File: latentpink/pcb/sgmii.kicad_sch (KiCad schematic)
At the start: 4 parts, among them J22 BEL_FUSE_0845-2R1T-E4, U2 XC7K160T-2FBG484C, U5 DP83867, U6 DP83867

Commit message: Initial start of DP83867 schematic
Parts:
- added C355, C356, C365, C366, C367, C368, C369, C370, C371, C372, C373, C374, C375, C376, C377, C378, C379, C380, C381, C382, C383, C384, C385, C386: 0.47 uF, azonenberg_pcb:EIA_0402_CAP_NOSILK, symbol device:C
- added C357, C358, C359, C360, C361, C362, C363, C364: 4.7 uF, azonenberg_pcb:EIA_0603_CAP_NOSILK, symbol device:C
- added R112, R?: 1.5K, symbol device:R
- added R113, R?: 2.2K, symbol device:R
- added R114, R?: 11K 1%, symbol device:R
- added R115, R116: 33, azonenberg_pcb:EIA_0402_RES_NOSILK, symbol device:R
- added R? (x2): R, symbol device:R
- added TP21, TP22: TESTPOINT, symbol conn:CONN_01X01
- added U7, U8: TBD, symbol osc-azonenberg:OSC
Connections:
- net GND: now reaches J22.1 (GND)
- net GND: now also J22.20 (GND), U5.PAD (GND), U6.PAD (GND), C355.2, C356.2, C357.2, C358.2, C359.2, C360.2, C361.2, C362.2, C363.2, C364.2, C365.2, C366.2, C367.2, C368.2, C369.2, C370.2, C371.2, C372.2, C373.2, C374.2, C375.2, C376.2, C377.2, C378.2, C379.2, C380.2, C381.2, C382.2, C383.2, C384.2, C385.2, C386.2, R114.1, R?.1, U7.2 (Vss), U8.2 (Vss)
- net ETH13_C_N: now reaches J22.10 (BI_DC_N)
- net ETH13_C_N: now also U5.8 (ETH_C_N)
- net ETH13_B_P: now reaches J22.11 (BI_DB_P)
- net ETH13_B_P: now also U5.4 (ETH_B_P)
- net ETH13_A_N: now reaches J22.13 (BI_DA_N)
- net ETH13_A_N: now also U5.2 (ETH_A_N)
- net ETH13_D_N: now reaches J22.2 (BI_DD_N)
- net ETH13_D_N: now also U5.11 (ETH_D_N)
- net ETH13_C_P: now reaches J22.3 (BI_DC_P)
- net ETH13_C_P: now also U5.7 (ETH_C_P)
- net ETH13_B_N: now reaches J22.5 (BI_DB_N)
- net ETH13_B_N: now also U5.5 (ETH_B_N)
- net ETH13_A_P: now reaches J22.6 (BI_DA_P)
- net ETH13_A_P: now also U5.1 (ETH_A_P)
- net ETH13_D_P: now reaches J22.9 (BI_DD_P)
- net ETH13_D_P: now also U5.10 (ETH_D_P)
- net ETH12_A_P: now reaches U6.1 (ETH_A_P)
- net ETH12_D_P: now reaches U6.10 (ETH_D_P)
- net ETH12_D_P: now also J22.26 (BI_DD_P)
- net ETH12_D_N: now reaches U6.11 (ETH_D_N)
- net ETH12_D_N: now also J22.19 (BI_DD_N)
- net at U6.12 (RBIAS): now also R114.2
- net DP_A1V8: now reaches U6.13 (A1V8)
- net DP_A1V8: now also U5.13 (A1V8), U5.48 (A1V8), U6.48 (A1V8), C359.1, C363.1, C367.1, C371.1, C374.1, C377.1
- net PHY_CLK_25MHZ_0: now reaches U6.15 (XI)
- net PHY_CLK_25MHZ_0: now also R115.2
- net DP_MDC: now reaches U6.16 (MDC)
- net DP_MDC: now also U2.AA6 (IO_L3P_T0_DQS_33), U5.16 (MDC)
- net DP_MDIO: now reaches U6.17 (MDIO)
- net DP_MDIO: now also U2.AB6 (IO_L3N_T0_DQS_33), U5.17 (MDIO), R112.2, R?.2
- net DP_CLKOUT0: now reaches U6.18 (CLK_OUT)
- net DP_CLKOUT0: now also TP21.1 (P1)
- net 1V8: now reaches U6.19 (VCCIO)
- net 1V8: now also U5.19 (VCCIO), U5.30 (VCCIO), U5.41 (VCCIO), U6.30 (VCCIO), U6.41 (VCCIO), C355.1, C356.1, R112.1, R113.1, R?.1, R?.1, U7.1 (E/D#), U7.4 (Vdd), U8.1 (E/D#), U8.4 (Vdd)
- net ETH12_A_N: now reaches U6.2 (ETH_A_N)
- net ETH12_A_N: now also J22.15 (BI_DA_P), J22.21 (BI_DA_N)
- net 1V0: now reaches U6.24 (1V0)
- net 1V0: now also U5.24 (1V0), U5.31 (1V0), U5.42 (1V0), U5.6 (1V0), U6.31 (1V0), U6.42 (1V0), U6.6 (1V0), C358.1, C362.1, C366.1, C370.1, C373.1, C376.1, C381.1, C383.1, C385.1, C386.1
- net ETH12_SGMII_TX_P: now reaches U6.27 (TX_D1/SGMII_TX_P)
- net ETH12_SGMII_TX_N: now reaches U6.28 (TX_D0/SGMII_TX_N)
- net DP_A2V5: now reaches U6.3 (A2V5)
- net DP_A2V5: now also U5.3 (A2V5), U5.9 (A2V5), U6.9 (A2V5), C357.1, C361.1, C365.1, C369.1, C379.1, C380.1
- net ETH12_SGMII_CLKOUT_P: now reaches U6.33 (RX_D0/SGMII_CLKOUT_P)
- net ETH12_SGMII_CLKOUT_N: now reaches U6.34 (RX_D1/SGMII_CLKOUT_N)
- net ETH12_SGMII_RX_P: now reaches U6.35 (RX_D2/SGMII_RX_P)
- net ETH12_SGMII_RX_N: now reaches U6.36 (RX_D3/SGMII_RX_N)
- net ETH12_RX_CTRL_STRAP: now reaches U6.38 (RX_CTRL)
- net ETH12_B_P: now reaches U6.4 (ETH_B_P)
- net ETH12_B_P: now also J22.23 (BI_DB_P)
- net ETH12_RST_N: now reaches U6.43 (~{RESET})
- net ETH12_RST_N: now also U2.AB7 (IO_L2N_T0_33)
- net ETH12_INT_N: now reaches U6.44 (~{INT}/~{PWRDN})
- net ETH12_INT_N: now also U2.AB8 (IO_L2P_T0_33), R113.2
- net ETH12_B_N: now reaches U6.5 (ETH_B_N)
- net ETH12_B_N: now also J22.16 (BI_DB_N)
- net ETH12_C_P: now reaches U6.7 (ETH_C_P)
- net ETH12_C_P: now also J22.18 (BI_DC_P)
- net ETH12_C_N: now reaches U6.8 (ETH_C_N)
- net ETH12_C_N: now also J22.24 (BI_DC_N)
- net at U5.12 (RBIAS): now also R?.2
- net PHY_CLK_25MHZ_1: now reaches U5.15 (XI)
- net PHY_CLK_25MHZ_1: now also R116.2
- net DP_CLKOUT1: now reaches U5.18 (CLK_OUT)
- net DP_CLKOUT1: now also TP22.1 (P1)
- net ETH13_SGMII_TX_P: now reaches U5.27 (TX_D1/SGMII_TX_P)
- net ETH13_SGMII_TX_N: now reaches U5.28 (TX_D0/SGMII_TX_N)
- net ETH13_SGMII_CLKOUT_P: now reaches U5.33 (RX_D0/SGMII_CLKOUT_P)
- net ETH13_SGMII_CLKOUT_N: now reaches U5.34 (RX_D1/SGMII_CLKOUT_N)
- net ETH13_SGMII_RX_P: now reaches U5.35 (RX_D2/SGMII_RX_P)
- net ETH13_SGMII_RX_N: now reaches U5.36 (RX_D3/SGMII_RX_N)
- net ETH13_RX_CTRL_STRAP: now reaches U5.38 (RX_CTRL)
- net ETH13_RST_N: now reaches U5.43 (~{RESET})
- net ETH13_RST_N: now also U2.AB5 (IO_L1N_T0_33)
- net ETH13_INT_N: now reaches U5.44 (~{INT}/~{PWRDN})
- net ETH13_INT_N: now also U2.AA5 (IO_L1P_T0_33), R?.2
- net at U2.T14 (IO_25_VRP_33): now also R?.2
- net at U2.T6 (IO_0_VRN_33): now also R?.2
- net CHGND: now reaches J22.SHLD
- new net: R116.1, U8.3 (CLK)
- new net: R115.1, U7.3 (CLK)
- new net D1V8: C360.1, C364.1, C368.1, C372.1, C375.1, C378.1, C382.1, C384.1
- no-connect marks 0 -> 12
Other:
- note added: "TODO: PHYADDR straps"
- note added: "TODO: ac coupling and/or biasing"
- note added: "TODO: power filtering"
- moved on the sheet: U2G

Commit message: Rearranged ports, added center tap capacitors
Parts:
- added C387, C388, C389, C390, C391, C392: 0.1 uF, azonenberg_pcb:EIA_0402_CAP_NOSILK, symbol device:C
- R117, R118: renamed from R?; value R -> 100
- gave numbers to parts that had none: 3
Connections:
- net D1V8 is gone; now on net 1V8_IO: C360.1, C364.1, C368.1, C372.1, C375.1, C378.1, C382.1, C384.1
- net 1V8: no longer C355.1, C356.1, U5.19 (VCCIO), U5.30 (VCCIO), U5.41 (VCCIO), U6.19 (VCCIO), U6.30 (VCCIO), U6.41 (VCCIO), U7.1 (E/D#), U7.4 (Vdd), U8.1 (E/D#), U8.4 (Vdd)
- net ETH12_SGMII_CLKOUT_N: now also C390.1
- net ETH12_SGMII_CLKOUT_P: now also C389.1
- net ETH12_SGMII_RX_N: now also C392.1
- net ETH12_SGMII_RX_P: now also C391.1
- net ETH12_SGMII_TX_N: now also C388.1
- net ETH12_SGMII_TX_P: now also C387.1
- net GND: now also R118.1
- net 1V8_IO: now reaches R117.1
- net 1V8_IO: now also C355.1, C356.1, U5.19 (VCCIO), U5.30 (VCCIO), U5.41 (VCCIO), U6.19 (VCCIO), U6.30 (VCCIO), U6.41 (VCCIO), U7.1 (E/D#), U7.4 (Vdd), U8.1 (E/D#), U8.4 (Vdd)
- net ETH12_SGMII_RX_AC_N: now reaches U2.U6 (IO_L10N_T1_33)
- net ETH12_SGMII_RX_AC_N: now also C392.2
- net ETH12_SGMII_RX_AC_P: now reaches U2.U7 (IO_L10P_T1_33)
- net ETH12_SGMII_RX_AC_P: now also C391.2
- net ETH12_SGMII_TX_AC_P: now reaches U2.V7 (IO_L11P_T1_SRCC_33)
- net ETH12_SGMII_TX_AC_P: now also C387.2
- net ETH12_SGMII_TX_AC_N: now reaches U2.W7 (IO_L11N_T1_SRCC_33)
- net ETH12_SGMII_TX_AC_N: now also C388.2
- net ETH12_SGMII_CLKOUT_AC_N: now reaches U2.Y7 (IO_L12N_T1_MRCC_33)
- net ETH12_SGMII_CLKOUT_AC_N: now also C390.2
- net ETH12_SGMII_CLKOUT_AC_P: now reaches U2.Y8 (IO_L12P_T1_MRCC_33)
- net ETH12_SGMII_CLKOUT_AC_P: now also C389.2
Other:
- note added: "SGMII AC coupling Hook up clocks just in case, but if we need them something is wrong."
- note added: "UG471 figure 1-10 Ext ref resistor = 2x Z0"
- note added: "Use DIFF_HSTL_I_DCI_18 for SGMII inputs Separate split terminations No biasing needed since termination provides bias to keep Vcm at Vccio/2"
- note removed: "TODO: ac coupling and/or biasing"
- moved on the sheet: R117, R118, U2G

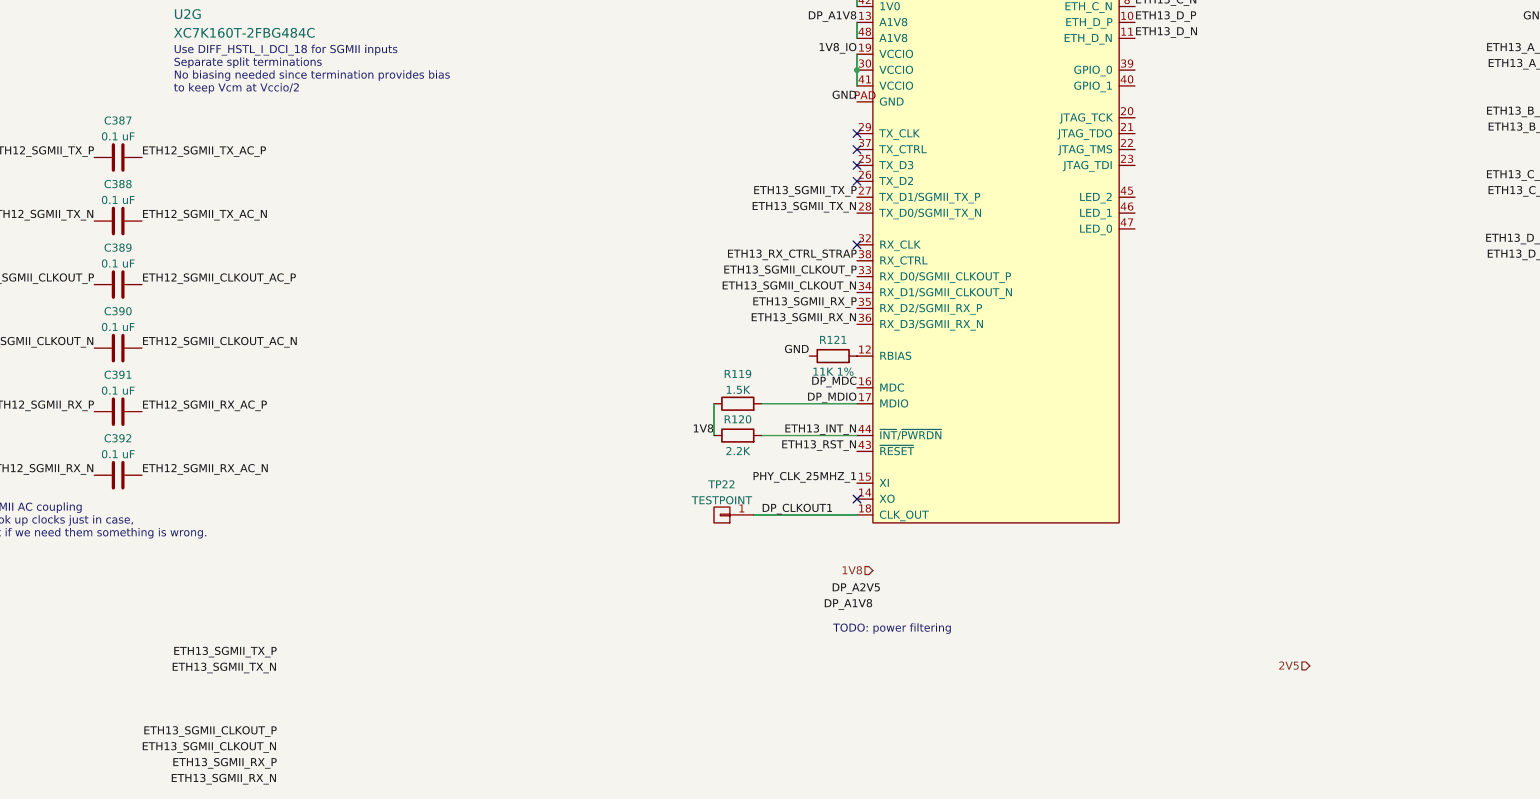
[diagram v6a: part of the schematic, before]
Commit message: Continued initial component placement
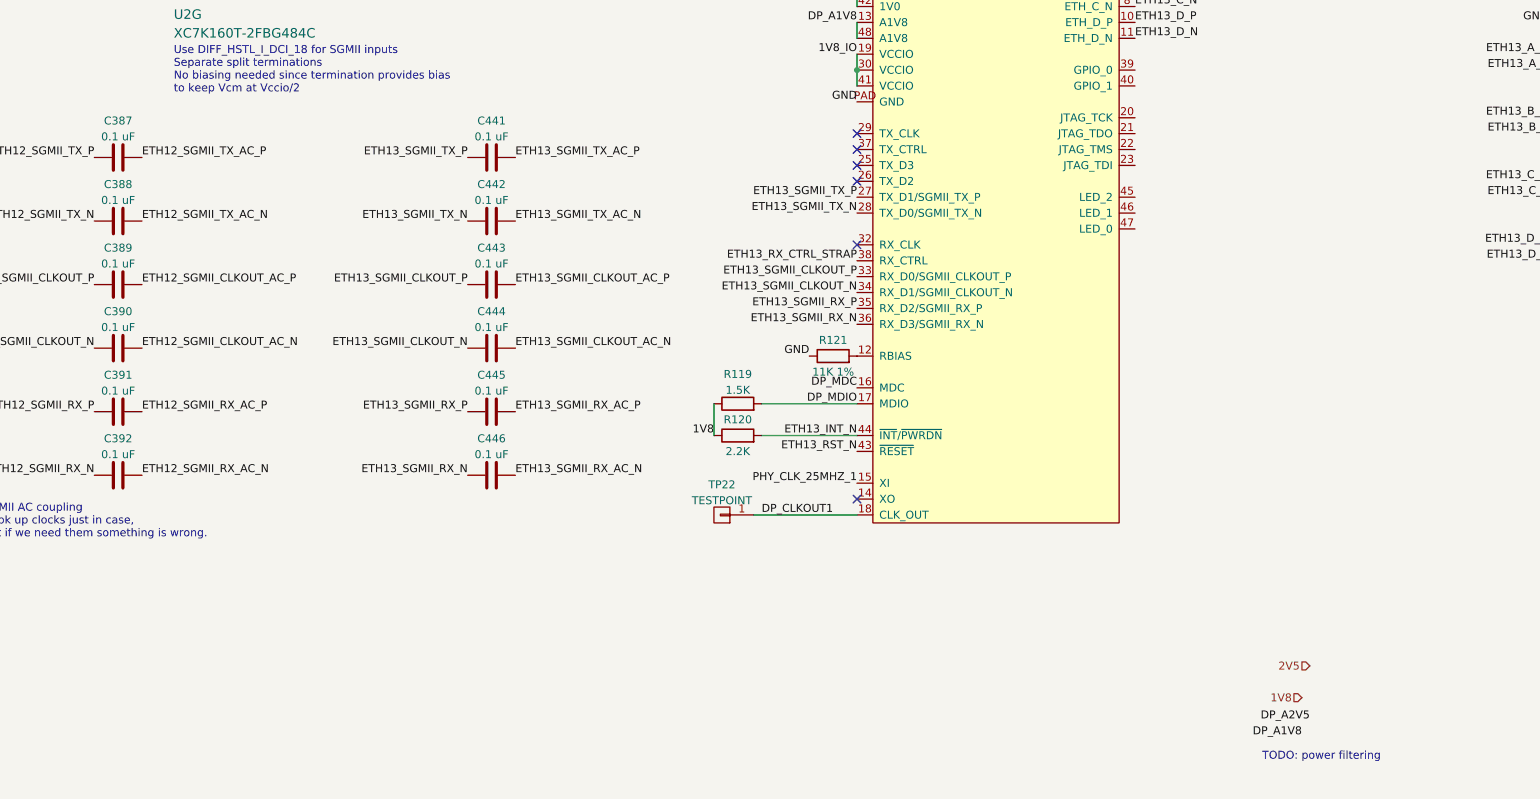
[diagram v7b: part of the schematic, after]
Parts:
- added C441, C442, C443, C444, C445, C446: 0.1 uF, azonenberg_pcb:EIA_0402_CAP_NOSILK, symbol device:C
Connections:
- net ETH13_SGMII_CLKOUT_N: now also C444.1
- net ETH13_SGMII_CLKOUT_P: now also C443.1
- net ETH13_SGMII_RX_N: now also C446.1
- net ETH13_SGMII_RX_P: now also C445.1
- net ETH13_SGMII_TX_N: now also C442.1
- net ETH13_SGMII_TX_P: now also C441.1
- new net ETH13_SGMII_CLKOUT_AC_N: C444.2
- new net ETH13_SGMII_CLKOUT_AC_P: C443.2
- new net ETH13_SGMII_RX_AC_N: C446.2
- new net ETH13_SGMII_RX_AC_P: C445.2
- new net ETH13_SGMII_TX_AC_N: C442.2
- new net ETH13_SGMII_TX_AC_P: C441.2
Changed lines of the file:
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@@
     (effects (font (size 1.27 1.27)) (justify left bottom))
   )
-  (text "TODO: power filtering" (at 154.94 254 0)
+  (text "TODO: power filtering" (at 223.52 274.32 0)
     (effects (font (size 1.27 1.27)) (justify left bottom))
   )
@@
     (effects (font (size 1.27 1.27)) (justify right bottom))
   )
-  (label "ETH13_SGMII_RX_P" (at 66.04 275.59 180)
+  (label "ETH13_SGMII_RX_P" (at 96.52 218.44 180)
     (effects (font (size 1.27 1.27)) (justify right bottom))
   )
@@
     (effects (font (size 1.27 1.27)) (justify right bottom))
   )
+  (label "ETH13_SGMII_TX_AC_P" (at 104.14 177.8 0)
+    (effects (font (size 1.27 1.27)) (justify left bottom))
+  )
   (label "ETH12_SGMII_CLKOUT_AC_N" (at 44.45 208.28 0)
     (effects (font (size 1.27 1.27)) (justify left bottom))
@@
     (effects (font (size 1.27 1.27)) (justify right bottom))
   )
+  (label "ETH13_SGMII_TX_AC_N" (at 104.14 187.96 0)
+    (effects (font (size 1.27 1.27)) (justify left bottom))
+  )
   (label "ETH12_SGMII_RX_P" (at 36.83 218.44 180)
     (effects (font (size 1.27 1.27)) (justify right bottom))
@@
     (effects (font (size 1.27 1.27)) (justify right bottom))
   )
-  (label "ETH13_SGMII_RX_N" (at 66.04 278.13 180)
+  (label "ETH13_SGMII_RX_N" (at 96.52 228.6 180)
     (effects (font (size 1.27 1.27)) (justify right bottom))
   )
@@
     (effects (font (size 1.27 1.27)) (justify right bottom))
   )
-  (label "ETH13_SGMII_TX_P" (at 66.04 257.81 180)
+  (label "ETH13_SGMII_RX_AC_N" (at 104.14 228.6 0)
+    (effects (font (size 1.27 1.27)) (justify left bottom))
+  )
+  (label "ETH13_SGMII_TX_P" (at 96.52 177.8 180)
     (effects (font (size 1.27 1.27)) (justify right bottom))
   )
@@
     (effects (font (size 1.27 1.27)) (justify left bottom))
   )
-  (label "ETH13_SGMII_CLKOUT_N" (at 66.04 273.05 180)
+  (label "ETH13_SGMII_CLKOUT_N" (at 96.52 208.28 180)
     (effects (font (size 1.27 1.27)) (justify right bottom))
   )
@@
     (effects (font (size 1.27 1.27)) (justify right bottom))
   )
-  (label "DP_A1V8" (at 161.29 250.19 180)
+  (label "DP_A1V8" (at 229.87 270.51 180)
     (effects (font (size 1.27 1.27)) (justify right bottom))
   )
@@
     (effects (font (size 1.27 1.27)) (justify right bottom))
   )
-  (label "ETH13_SGMII_TX_N" (at 66.04 260.35 180)
+  (label "ETH13_SGMII_TX_N" (at 96.52 187.96 180)
     (effects (font (size 1.27 1.27)) (justify right bottom))
   )
@@
     (effects (font (size 1.27 1.27)) (justify left bottom))
   )
-  (label "ETH13_SGMII_CLKOUT_P" (at 66.04 270.51 180)
+  (label "ETH13_SGMII_CLKOUT_P" (at 96.52 198.12 180)
     (effects (font (size 1.27 1.27)) (justify right bottom))
   )
@@
     (effects (font (size 1.27 1.27)) (justify right bottom))
   )
+  (label "ETH13_SGMII_CLKOUT_AC_N" (at 104.14 208.28 0)
+    (effects (font (size 1.27 1.27)) (justify left bottom))
+  )
   (label "ETH13_B_P" (at 269.24 173.99 180)
     (effects (font (size 1.27 1.27)) (justify right bottom))
   )
+  (label "ETH13_SGMII_CLKOUT_AC_P" (at 104.14 198.12 0)
+    (effects (font (size 1.27 1.27)) (justify left bottom))
+  )
   (label "1V8" (at 135.89 222.25 180)
     (effects (font (size 1.27 1.27)) (justify right bottom))
@@
     (effects (font (size 1.27 1.27)) (justify right bottom))
   )
-  (label "DP_A2V5" (at 162.56 247.65 180)
+  (label "DP_A2V5" (at 231.14 267.97 180)
     (effects (font (size 1.27 1.27)) (justify right bottom))
   )
@@
   )
   (label "ETH12_SGMII_RX_AC_N" (at 44.45 228.6 0)
+    (effects (font (size 1.27 1.27)) (justify left bottom))
+  )
+  (label "ETH13_SGMII_RX_AC_P" (at 104.14 218.44 0)
     (effects (font (size 1.27 1.27)) (justify left bottom))
   )
@@
     (effects (font (size 1.27 1.27)) (justify right))
   )
-  (hierarchical_label "1V8" (shape input) (at 161.29 243.84 180)
+  (hierarchical_label "1V8" (shape input) (at 229.87 264.16 180)
     (effects (font (size 1.27 1.27)) (justify right))
   )
@@
     (pin "1")
   )
+  (symbol (lib_id "device:C") (at 100.33 218.44 90) (unit 1)
+    (in_bom yes) (on_board yes) (fields_autoplaced)
+    (property "Reference" "C445" (id 0) (at 100.33 212.5812 90))
+    (property "Value" "0.1 uF" (id 1) (at 100.33 215.1181 90))
+    (property "Footprint" "azonenberg_pcb:EIA_0402_CAP_NOSILK" (id 2) (at 104.14 217.4748 0)
+      (effects (font (size 1.27 1.27)) hide)
+    )
+    (property "Datasheet" "" (id 3) (at 100.33 218.44 0)
+      (effects (font (size 1.27 1.27)) hide)
+    )
+    (pin "1")
+    (pin "2")
+  )
   (symbol (lib_id "device:R") (at 139.7 217.17 90) (unit 1)
     (in_bom yes) (on_board yes) (fields_autoplaced)
@@
     )
     (property "Datasheet" "" (id 3) (at 353.06 43.18 0)
+      (effects (font (size 1.27 1.27)) hide)
+    )
+    (pin "1")
+    (pin "2")
+  )
+  (symbol (lib_id "device:C") (at 100.33 177.8 90) (unit 1)
+    (in_bom yes) (on_board yes) (fields_autoplaced)
+    (property "Reference" "C441" (id 0) (at 100.33 171.9412 90))
+    (property "Value" "0.1 uF" (id 1) (at 100.33 174.4781 90))
+    (property "Footprint" "azonenberg_pcb:EIA_0402_CAP_NOSILK" (id 2) (at 104.14 176.8348 0)
+      (effects (font (size 1.27 1.27)) hide)
+    )
+    (property "Datasheet" "" (id 3) (at 100.33 177.8 0)
       (effects (font (size 1.27 1.27)) hide)
     )
@@
     (pin "PAD")
   )
+  (symbol (lib_id "device:C") (at 100.33 228.6 90) (unit 1)
+    (in_bom yes) (on_board yes) (fields_autoplaced)
+    (property "Reference" "C446" (id 0) (at 100.33 222.7412 90))
+    (property "Value" "0.1 uF" (id 1) (at 100.33 225.2781 90))
+    (property "Footprint" "azonenberg_pcb:EIA_0402_CAP_NOSILK" (id 2) (at 104.14 227.6348 0)
+      (effects (font (size 1.27 1.27)) hide)
+    )
+    (property "Datasheet" "" (id 3) (at 100.33 228.6 0)
+      (effects (font (size 1.27 1.27)) hide)
+    )
+    (pin "1")
+    (pin "2")
+  )
   (symbol (lib_id "device:C") (at 327.66 157.48 0) (unit 1)
     (in_bom yes) (on_board yes) (fields_autoplaced)
@@
     )
     (property "Datasheet" "" (id 3) (at 327.66 87.63 0)
+      (effects (font (size 1.27 1.27)) hide)
+    )
+    (pin "1")
+    (pin "2")
+  )
+  (symbol (lib_id "device:C") (at 100.33 208.28 90) (unit 1)
+    (in_bom yes) (on_board yes) (fields_autoplaced)
+    (property "Reference" "C444" (id 0) (at 100.33 202.4212 90))
+    (property "Value" "0.1 uF" (id 1) (at 100.33 204.9581 90))
+    (property "Footprint" "azonenberg_pcb:EIA_0402_CAP_NOSILK" (id 2) (at 104.14 207.3148 0)
+      (effects (font (size 1.27 1.27)) hide)
+    )
+    (property "Datasheet" "" (id 3) (at 100.33 208.28 0)
       (effects (font (size 1.27 1.27)) hide)
     )
@@
     (pin "2")
   )
+  (symbol (lib_id "device:C") (at 100.33 187.96 90) (unit 1)
+    (in_bom yes) (on_board yes) (fields_autoplaced)
+    (property "Reference" "C442" (id 0) (at 100.33 182.1012 90))
+    (property "Value" "0.1 uF" (id 1) (at 100.33 184.6381 90))
+    (property "Footprint" "azonenberg_pcb:EIA_0402_CAP_NOSILK" (id 2) (at 104.14 186.9948 0)
+      (effects (font (size 1.27 1.27)) hide)
+    )
+    (property "Datasheet" "" (id 3) (at 100.33 187.96 0)
+      (effects (font (size 1.27 1.27)) hide)
+    )
+    (pin "1")
+    (pin "2")
+  )
   (symbol (lib_id "device:C") (at 40.64 177.8 90) (unit 1)
     (in_bom yes) (on_board yes) (fields_autoplaced)
@@
     (pin "9")
   )
+  (symbol (lib_id "device:C") (at 100.33 198.12 90) (unit 1)
+    (in_bom yes) (on_board yes) (fields_autoplaced)
+    (property "Reference" "C443" (id 0) (at 100.33 192.2612 90))
+    (property "Value" "0.1 uF" (id 1) (at 100.33 194.7981 90))
+    (property "Footprint" "azonenberg_pcb:EIA_0402_CAP_NOSILK" (id 2) (at 104.14 197.1548 0)
+      (effects (font (size 1.27 1.27)) hide)
+    )
+    (property "Datasheet" "" (id 3) (at 100.33 198.12 0)
+      (effects (font (size 1.27 1.27)) hide)
+    )
+    (pin "1")
+    (pin "2")
+  )
   (symbol (lib_id "device:C") (at 365.76 66.04 0) (unit 1)
